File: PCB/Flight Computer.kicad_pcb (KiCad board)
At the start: 6 copper layers, 30 x 60 mm, 80 parts, among them J501 Conn_02x03_Counter_Clockwise, J502 USB_C_Receptacle_USB2.0_16P, J503 Screw_Terminal_01x06, J504 Screw_Terminal_01x04, J505 Conn_01x04, J506 Conn_02x03_Counter_Clockwise, J507 Conn_01x05, J601 Conn_Coaxial, U201 LM1117MP-3.3, U301 W25Q128JVS, U302 STM32F446RETx, U401 MMC5633NJL, U402 LSM6DSV320, U403 MS5607-02BA, U404 SAM-M8Q, U601 RFM95W-915S2, Y301 Resonator

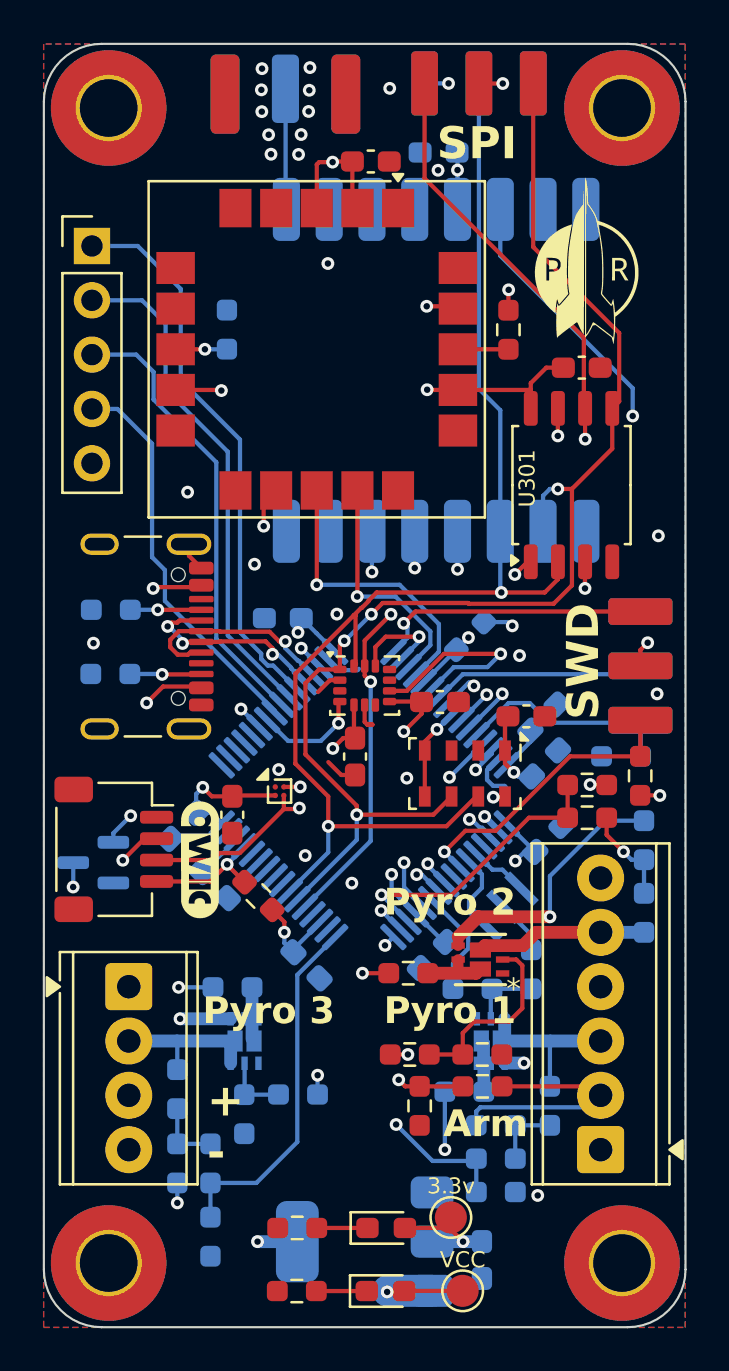
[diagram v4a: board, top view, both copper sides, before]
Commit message: Switch from high side switch to low side switch for pyro channels
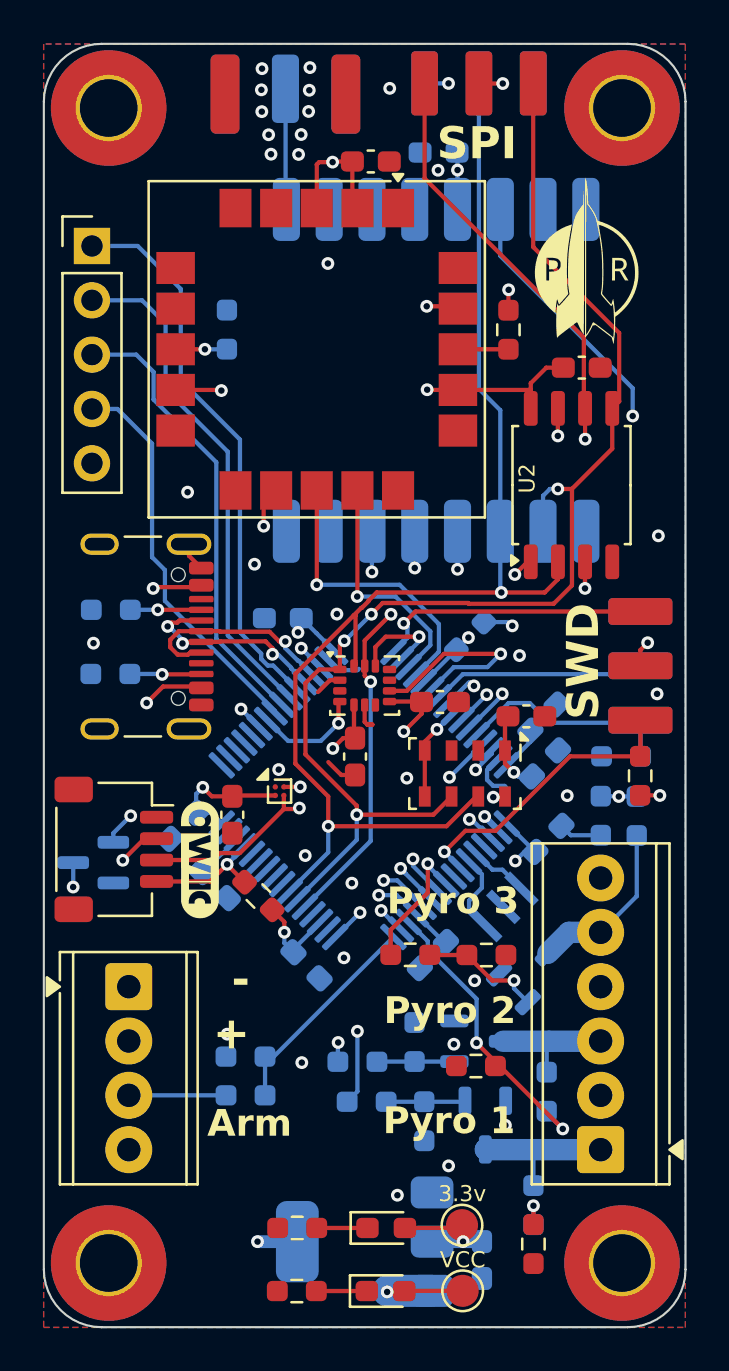
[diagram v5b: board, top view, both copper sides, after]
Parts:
- removed R701, R702, R703, R707, R708, R709, R712, R713, R714, R717: 10k, Resistor_SMD:R_0603_1608Metric_Pad0.98x0.95mm_HandSolder
- removed R704, R710, R715: 500, Resistor_SMD:R_0603_1608Metric_Pad0.98x0.95mm_HandSolder
- removed R705: 1k, Resistor_SMD:R_0603_1608Metric_Pad0.98x0.95mm_HandSolder
- removed R706, R711, R716, R719, R721, R723: 3k, Resistor_SMD:R_0603_1608Metric_Pad0.98x0.95mm_HandSolder
- removed R718, R720, R722: 5.1k, Resistor_SMD:R_0603_1608Metric_Pad0.98x0.95mm_HandSolder
- removed U701, U702, U703: ~, imported:TRANS_UT6J3_ROM
- added Q1: SL2302S, Package_TO_SOT_SMD:SOT-23-3, B.Cu at (118.3, 103.1)
- added Q2: SL2302S, Package_TO_SOT_SMD:SOT-23-3, B.Cu at (118.0, 99.1)
- added Q3: SL2302S, Package_TO_SOT_SMD:SOT-23-3, B.Cu at (120.4, 95.8)
- added R11: 10k, Resistor_SMD:R_0603_1608Metric_Pad0.98x0.95mm_HandSolder, B.Cu at (107.1, 101.7)
- added R12: 500, Resistor_SMD:R_0603_1608Metric_Pad0.98x0.95mm_HandSolder, B.Cu at (112.8, 102.0)
- added R13: 5.1k, Resistor_SMD:R_0603_1608Metric_Pad0.98x0.95mm_HandSolder, B.Cu at (120.6, 106.8)
- added R14: 1k, Resistor_SMD:R_0603_1608Metric_Pad0.98x0.95mm_HandSolder, B.Cu at (107.1, 99.8)
- added R15: 10k, Resistor_SMD:R_0603_1608Metric_Pad0.98x0.95mm_HandSolder, B.Cu at (115.5, 102.9)
- added R16: 3k, Resistor_SMD:R_0603_1608Metric_Pad0.98x0.95mm_HandSolder, F.Cu at (120.6, 108.6)
- added R17: 500, Resistor_SMD:R_0603_1608Metric_Pad0.98x0.95mm_HandSolder, B.Cu at (112.3, 100.1)
- added R18: 5.1k, Resistor_SMD:R_0603_1608Metric_Pad0.98x0.95mm_HandSolder, B.Cu at (121.2, 101.5)
- added R19: 10k, Resistor_SMD:R_0603_1608Metric_Pad0.98x0.95mm_HandSolder, B.Cu at (115.0, 99.2)
- added R20: 3k, Resistor_SMD:R_0603_1608Metric_Pad0.98x0.95mm_HandSolder, F.Cu at (117.9, 100.3)
- added R21: 500, Resistor_SMD:R_0603_1608Metric_Pad0.98x0.95mm_HandSolder, F.Cu at (114.8, 95.1)
- added R22: 5.1k, Resistor_SMD:R_0603_1608Metric_Pad0.98x0.95mm_HandSolder, B.Cu at (125.4, 88.6)
- added R23: 10k, Resistor_SMD:R_0603_1608Metric_Pad0.98x0.95mm_HandSolder, F.Cu at (118.4, 95.1)
- added R24: 3k, Resistor_SMD:R_0603_1608Metric_Pad0.98x0.95mm_HandSolder, B.Cu at (123.7, 88.6)
- moved TP2 0.63 mm to (117.2, 107.7)
- renumbered C201 to C1, C309 to C10, C401 to C11, C402 to C12, C403 to C13, C404 to C14, C405 to C15, C601 to C16, C301 to C2, C302 to C3, C303 to C4, C304 to C5, C305 to C6, C306 to C7, C307 to C8, C308 to C9, D201 to D1, D202 to D2, D501 to D3, G501 to G1, H501 to H1, H502 to H2, H503 to H3, H504 to H4, J501 to J1, J504 to J2, J502 to J3, J503 to J4, J505 to J5, J506 to J6, J507 to J7, J601 to J8, R201 to R1, R502 to R10, R202 to R2, R301 to R3, R302 to R4, R303 to R5, R304 to R6, R401 to R7, R402 to R8, R501 to R9, TP201 to TP1, TP202 to TP2, U201 to U1, U301 to U2, U302 to U3, U401 to U4, U402 to U5, U403 to U6, U404 to U7, U601 to U8, Y301 to Y1
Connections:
- J1 pad 3: GND -> unconnected-(J1-Pin_3-Pad3)
- J2 pad 2: /Pyro3 -> VCC
- J2 pad 3: GND -> Pyro_Power
- J4 pad 1: VCC -> /Pyro1
- J4 pad 3: /Pyro1 -> /Pyro2
- J4 pad 4: GND -> Pyro_Power
- J4 pad 5: /Pyro2 -> /Pyro3
- J4 pad 6: GND -> Pyro_Power
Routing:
- net VCC: track 72.1 -> 43.1 mm, vias 5 -> 2
- net Pyro_Power: track 68.4 -> 44.6 mm, vias 4 -> 0
- net /Pyro3_Trigger: track 15.4 -> 6.30 mm, vias 2 -> 1
- net Net-(U702A-G): track 8.87 -> 0.00 mm
- net /Pyro1_Trigger: track 5.20 -> 14.0 mm, vias 0 -> 2
- net Net-(Q3-G): track 0.00 -> 5.72 mm, vias 0 -> 1
- net Net-(R709-Pad2): track 4.60 -> 0.00 mm, vias 1 -> 0
- net Net-(Q1-G): track 0.00 -> 3.71 mm
- net Net-(Q2-G): track 0.00 -> 3.62 mm
- net Net-(U702B-G): track 3.47 -> 0.00 mm
- net Net-(R703-Pad2): track 3.26 -> 0.00 mm
- net Net-(U701A-G): track 3.25 -> 0.00 mm
- net Net-(R714-Pad2): track 3.20 -> 0.00 mm
- net Net-(U703A-G): track 3.08 -> 0.00 mm
- net /Pyro2_Trigger: track 10.8 -> 13.8 mm
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
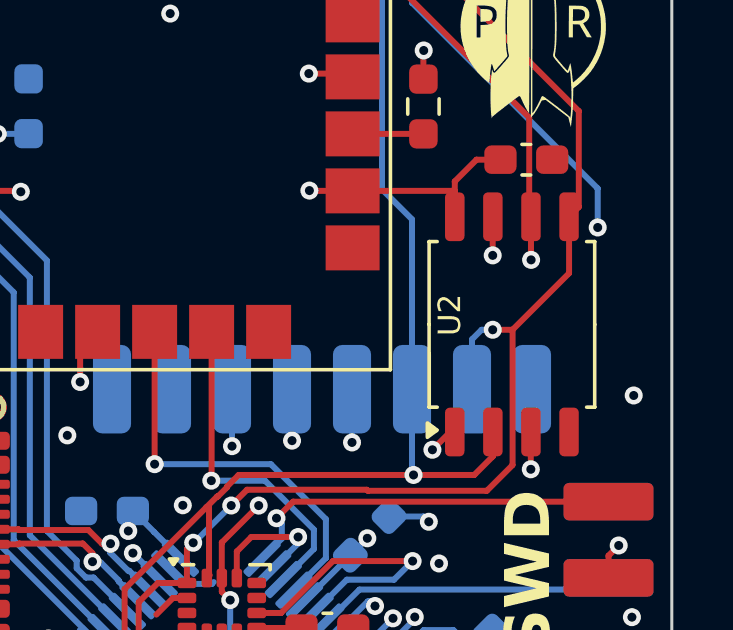
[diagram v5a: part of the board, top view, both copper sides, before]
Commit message: Fixed component annotation Updated BOM to reflect the pyro channel changes Updates Production files
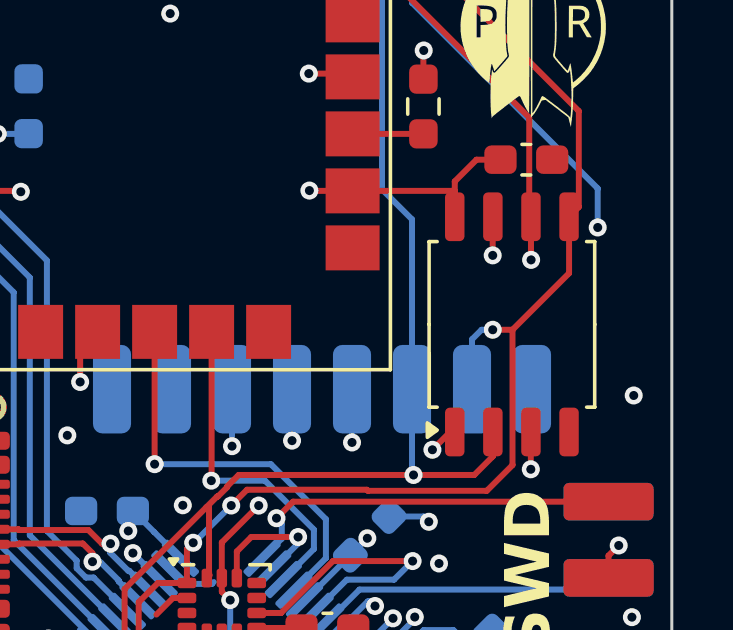
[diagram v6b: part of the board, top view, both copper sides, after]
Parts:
- renumbered C1 to C201, C2 to C301, C3 to C302, C4 to C303, C5 to C304, C6 to C305, C7 to C306, C8 to C307, C9 to C308, C10 to C309, C11 to C401, C12 to C402, C13 to C403, C14 to C404, C15 to C405, C16 to C601, D1 to D201, D2 to D202, D3 to D501, G1 to G501, H1 to H501, H2 to H502, H3 to H503, H4 to H504, J1 to J501, J3 to J502, J4 to J503, J2 to J504, J5 to J505, J6 to J506, J7 to J507, J8 to J601, Q1 to Q701, Q2 to Q702, Q3 to Q703, R1 to R201, R2 to R202, R3 to R301, R4 to R302, R5 to R303, R6 to R304, R7 to R401, R8 to R402, R9 to R501, R10 to R502, R11 to R701, R12 to R702, R13 to R703, R14 to R704, R15 to R705, R16 to R706, R17 to R707, R18 to R708, R19 to R709, R20 to R710, R21 to R711, R22 to R712, R23 to R713, R24 to R714, TP1 to TP201, TP2 to TP202, U1 to U201, U2 to U301, U3 to U302, U4 to U401, U5 to U402, U6 to U403, U7 to U404, U8 to U601, Y1 to Y301

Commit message: grounded programming interface
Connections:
- net /MCU/PB11 renamed /Buzzer
- net /MCU/PB12 renamed /MCU_LED
- J501 pad 3: unconnected-(J501-Pin_3-Pad3) -> GND
- U301 pad 2: /SPI_MOSI -> /SPI_MISO
- U301 pad 5: /SPI_MISO -> /SPI_MOSI
- U302 pad 35: /MCU/PB13 -> /MCU/PB14
- U302 pad 36: /MCU/PB14 -> /MCU/PB15
- U402 pad 1: /SPI_MISO -> /SPI_MOSI
- U402 pad 14: /SPI_MOSI -> /SPI_MISO

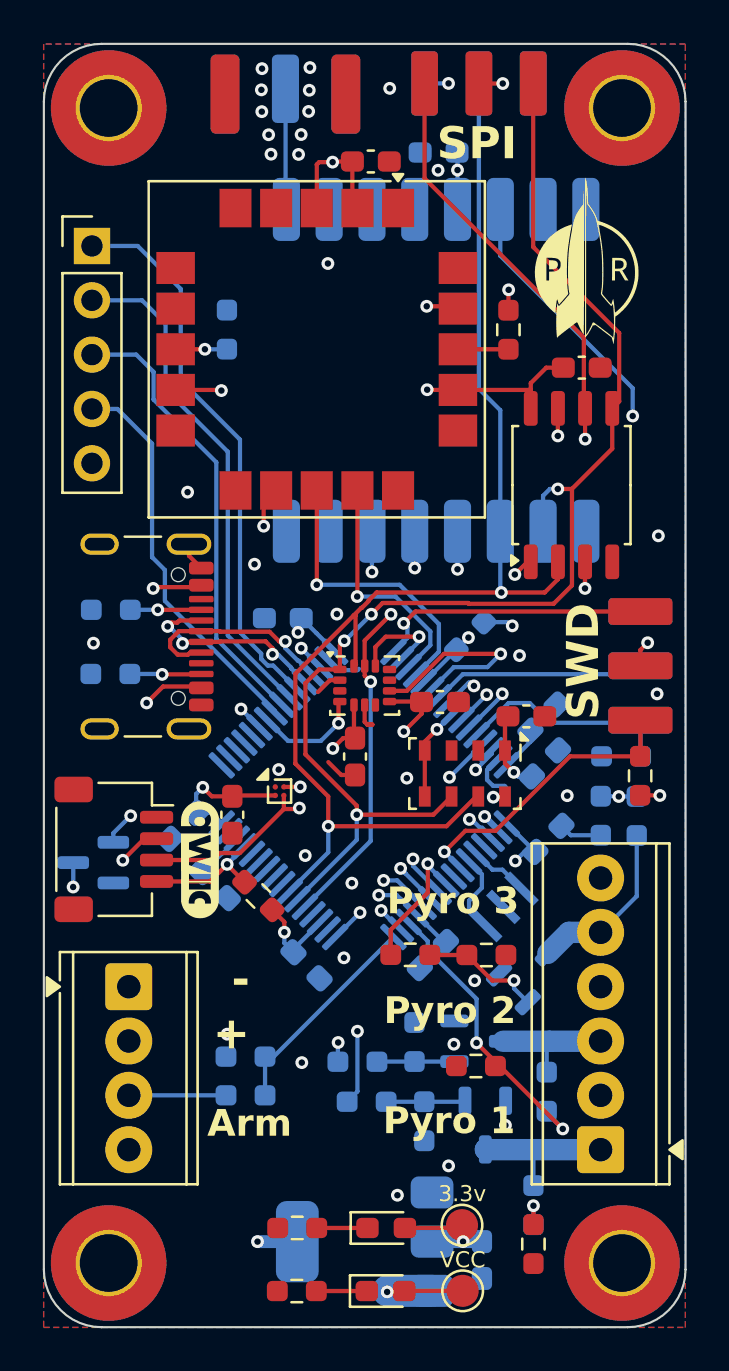
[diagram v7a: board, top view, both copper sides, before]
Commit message: - Updated schematic with solutions to the hardware problems - Remove files that are the .gitignore
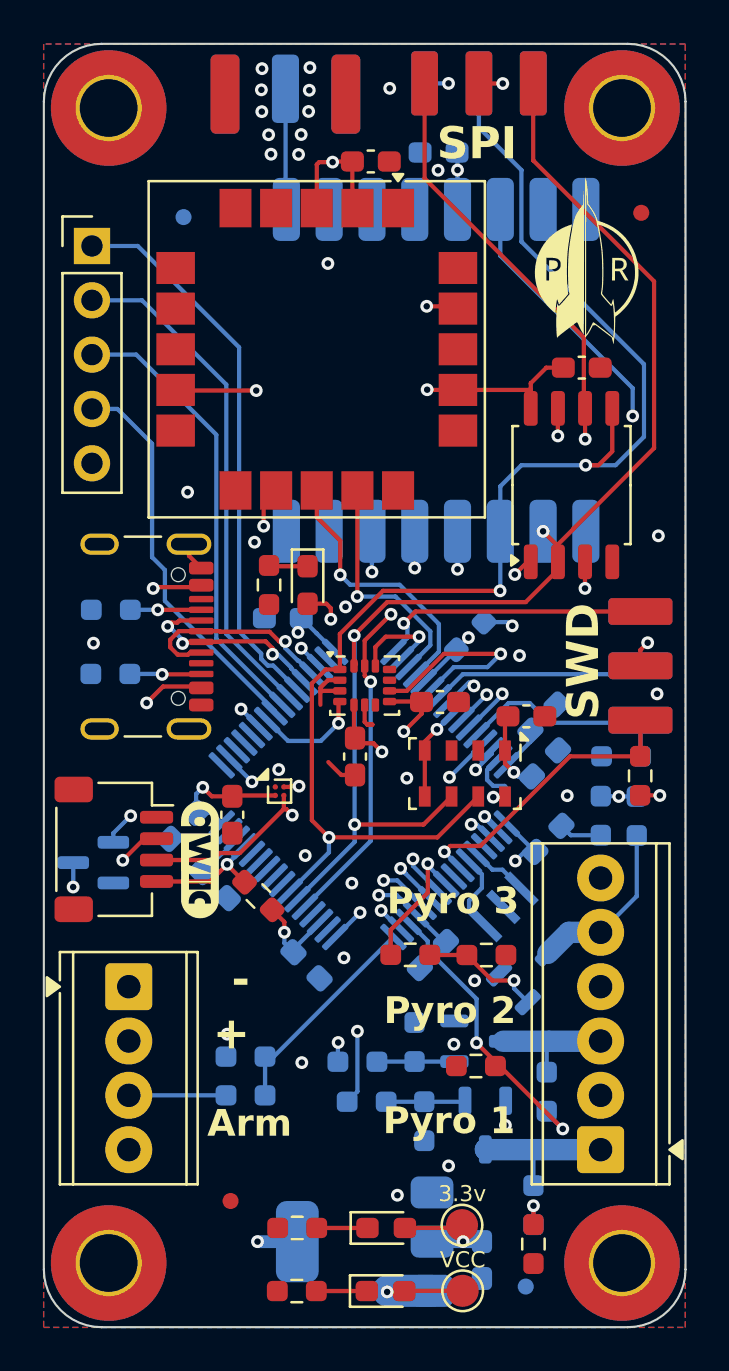
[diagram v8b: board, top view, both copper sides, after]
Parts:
- removed R401, R402: 10k, Resistor_SMD:R_0603_1608Metric_Pad0.98x0.95mm_HandSolder
- added D301: LED, LED_SMD:LED_0603_1608Metric_Pad1.05x0.95mm_HandSolder, F.Cu at (110.0, 77.8)
- added FID101: Fiducial, Fiducial:Fiducial_0.75mm_Mask1.5mm, F.Cu at (125.6, 60.4)
- added FID102: Fiducial, Fiducial:Fiducial_0.75mm_Mask1.5mm, F.Cu at (106.4, 106.6)
- added FID103: Fiducial, Fiducial:Fiducial_0.75mm_Mask1.5mm, B.Cu at (104.2, 60.6)
- added FID104: Fiducial, Fiducial:Fiducial_0.75mm_Mask1.5mm, B.Cu at (120.2, 110.6)
- added R305: 1k, Resistor_SMD:R_0603_1608Metric_Pad0.98x0.95mm_HandSolder, F.Cu at (108.2, 77.8)
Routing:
- net /MCU_LED: track 0.00 -> 13.5 mm, vias 0 -> 2
- net /SPI_MOSI: track 61.0 -> 66.1 mm, vias 2 -> 3
- net //GPS_SAFEBOOT: track 2.40 -> 0.00 mm, vias 1 -> 0
- net //GPS_RESET: track 2.36 -> 0.00 mm
- net Net-(D301-K): track 0.00 -> 1.82 mm
- net /SPI_MISO: track 61.3 -> 59.7 mm, vias 4 -> 3
- net /I2C_SDA: track 41.0 -> 42.2 mm
- net /GPS_TX: track 13.7 -> 12.8 mm
- net +3.3V: track 65.2 -> 64.5 mm, vias 18 -> 17
- net GND: track 14.1 -> 14.6 mm
